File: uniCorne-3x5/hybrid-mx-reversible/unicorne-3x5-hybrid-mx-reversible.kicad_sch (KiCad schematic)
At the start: 87 parts, among them J1 MJ-4PP-9, J2 Nice!View, J3 Conn_01x02, J3 Conn_01x03, SW1 SW_MX_HS, SW10 SW_MX_HS, SW11 SW_MX_HS, SW12 SW_MX_HS, SW13 SW_MX_HS, SW14 SW_MX_HS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

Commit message: amended hybrid 3x5
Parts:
- U1: footprint TB2086_MISC:ProMicro-ish-dn-rev-unrouted_3x5 -> TB2086_MISC:ProMicro-ish-dn-rev-unrouted_3x6
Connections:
- net BAT+: now also PSW1.1 (A); no longer PSW1.3 (C)

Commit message: fixed footprint for promicro-ish 3x6
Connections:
- net CS: now also U1.12 (B5); no longer U1.13 (B6)
- net IS_LEFT: now also U1.13 (B6); no longer U1.12 (B5)
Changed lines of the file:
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@@
     )
   )
-  (global_label "CS" (shape input) (at 80.645 54.61 0) (fields_autoplaced)
+  (global_label "IS_LEFT" (shape input) (at 80.645 54.61 0) (fields_autoplaced)
     (effects (font (size 1.1938 1.1938)) (justify left))
-    (property "Intersheetrefs" "${INTERSHEET_REFS}" (at 85.7069 54.61 0)
+    (property "Intersheetrefs" "${INTERSHEET_REFS}" (at 89.9706 54.61 0)
       (effects (font (size 1.27 1.27)) (justify left) hide)
     )
@@
     )
   )
-  (global_label "IS_LEFT" (shape input) (at 36.83 54.61 180) (fields_autoplaced)
+  (global_label "CS" (shape input) (at 36.83 54.61 180) (fields_autoplaced)
     (effects (font (size 1.1938 1.1938)) (justify right))
-    (property "Intersheetrefs" "${INTERSHEET_REFS}" (at 27.5044 54.61 0)
+    (property "Intersheetrefs" "${INTERSHEET_REFS}" (at 31.7681 54.61 0)
       (effects (font (size 1.27 1.27)) (justify right) hide)
     )

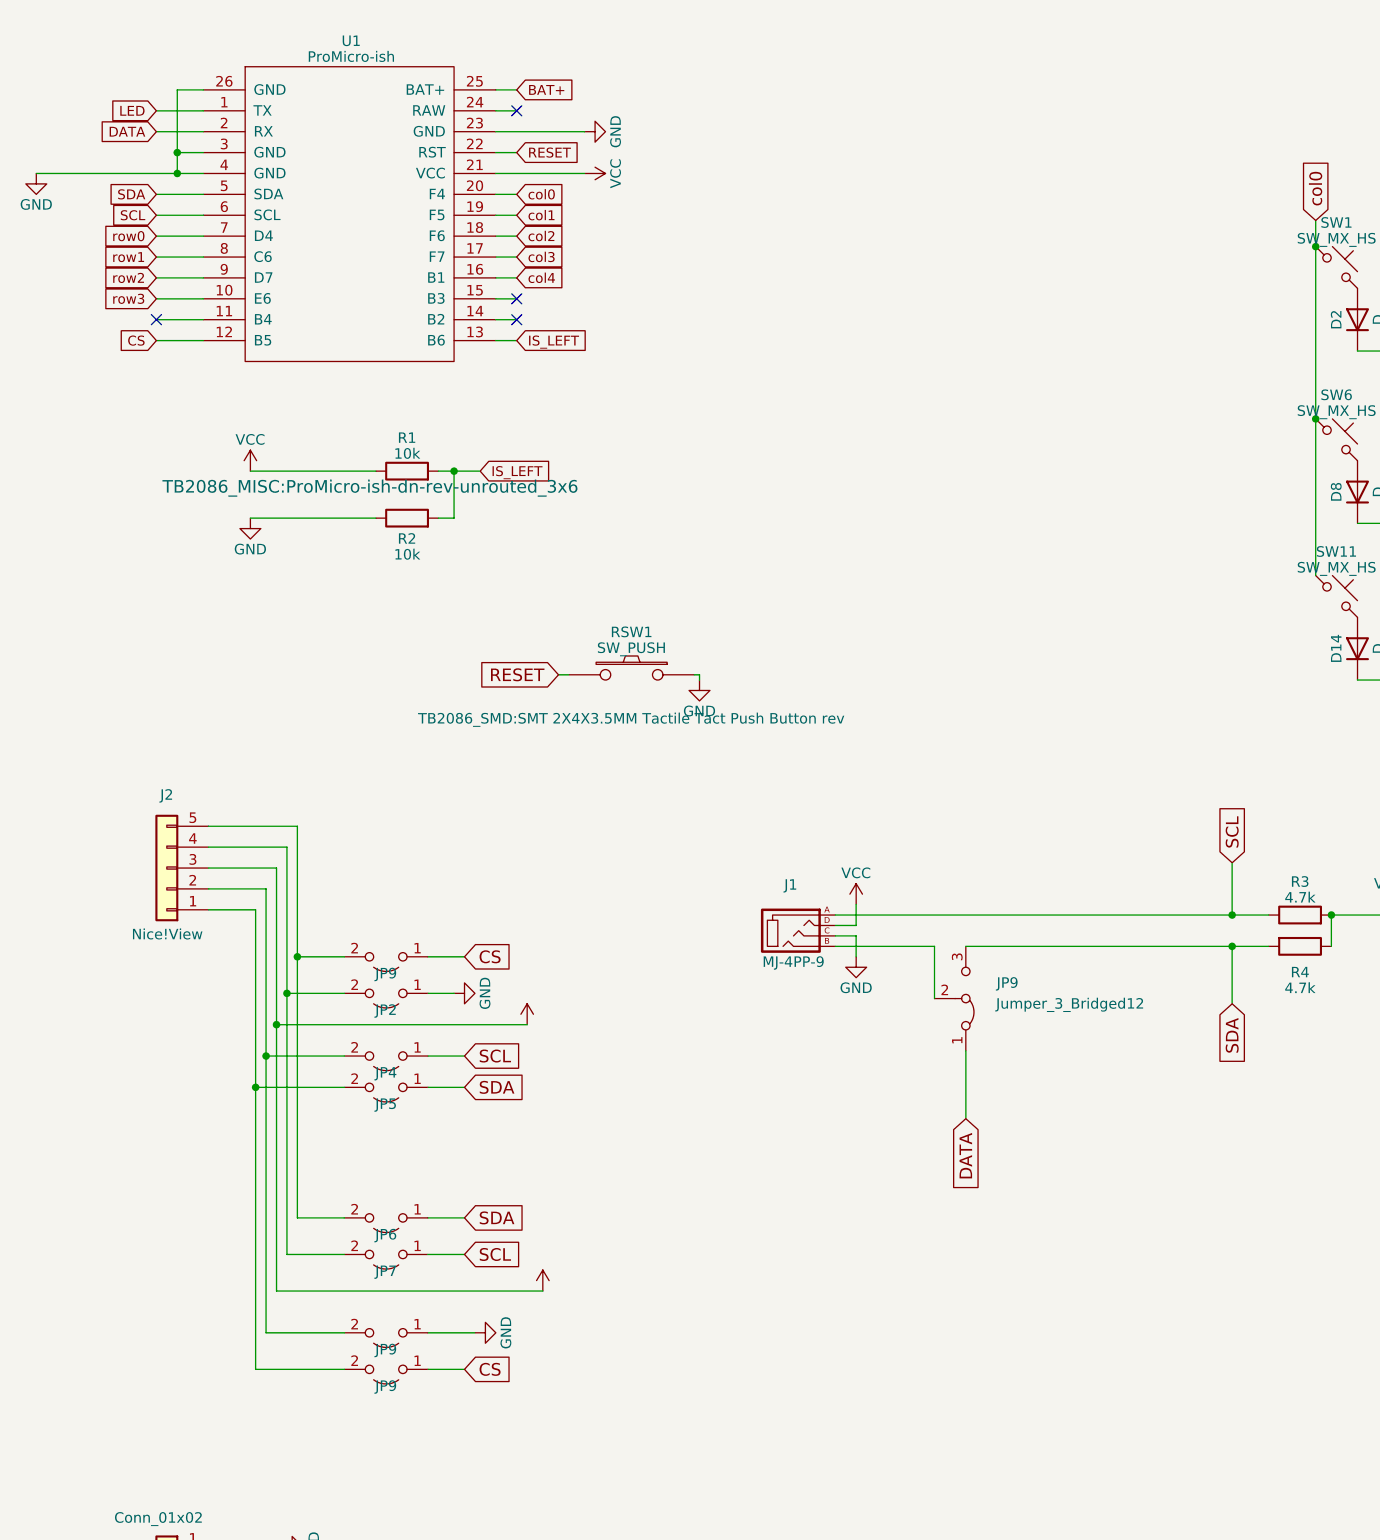
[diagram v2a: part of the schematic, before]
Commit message: Bug fix scl (#3)
* fixed 3x5 hyprid mx

* fixed 3x5

* fixed 3x6
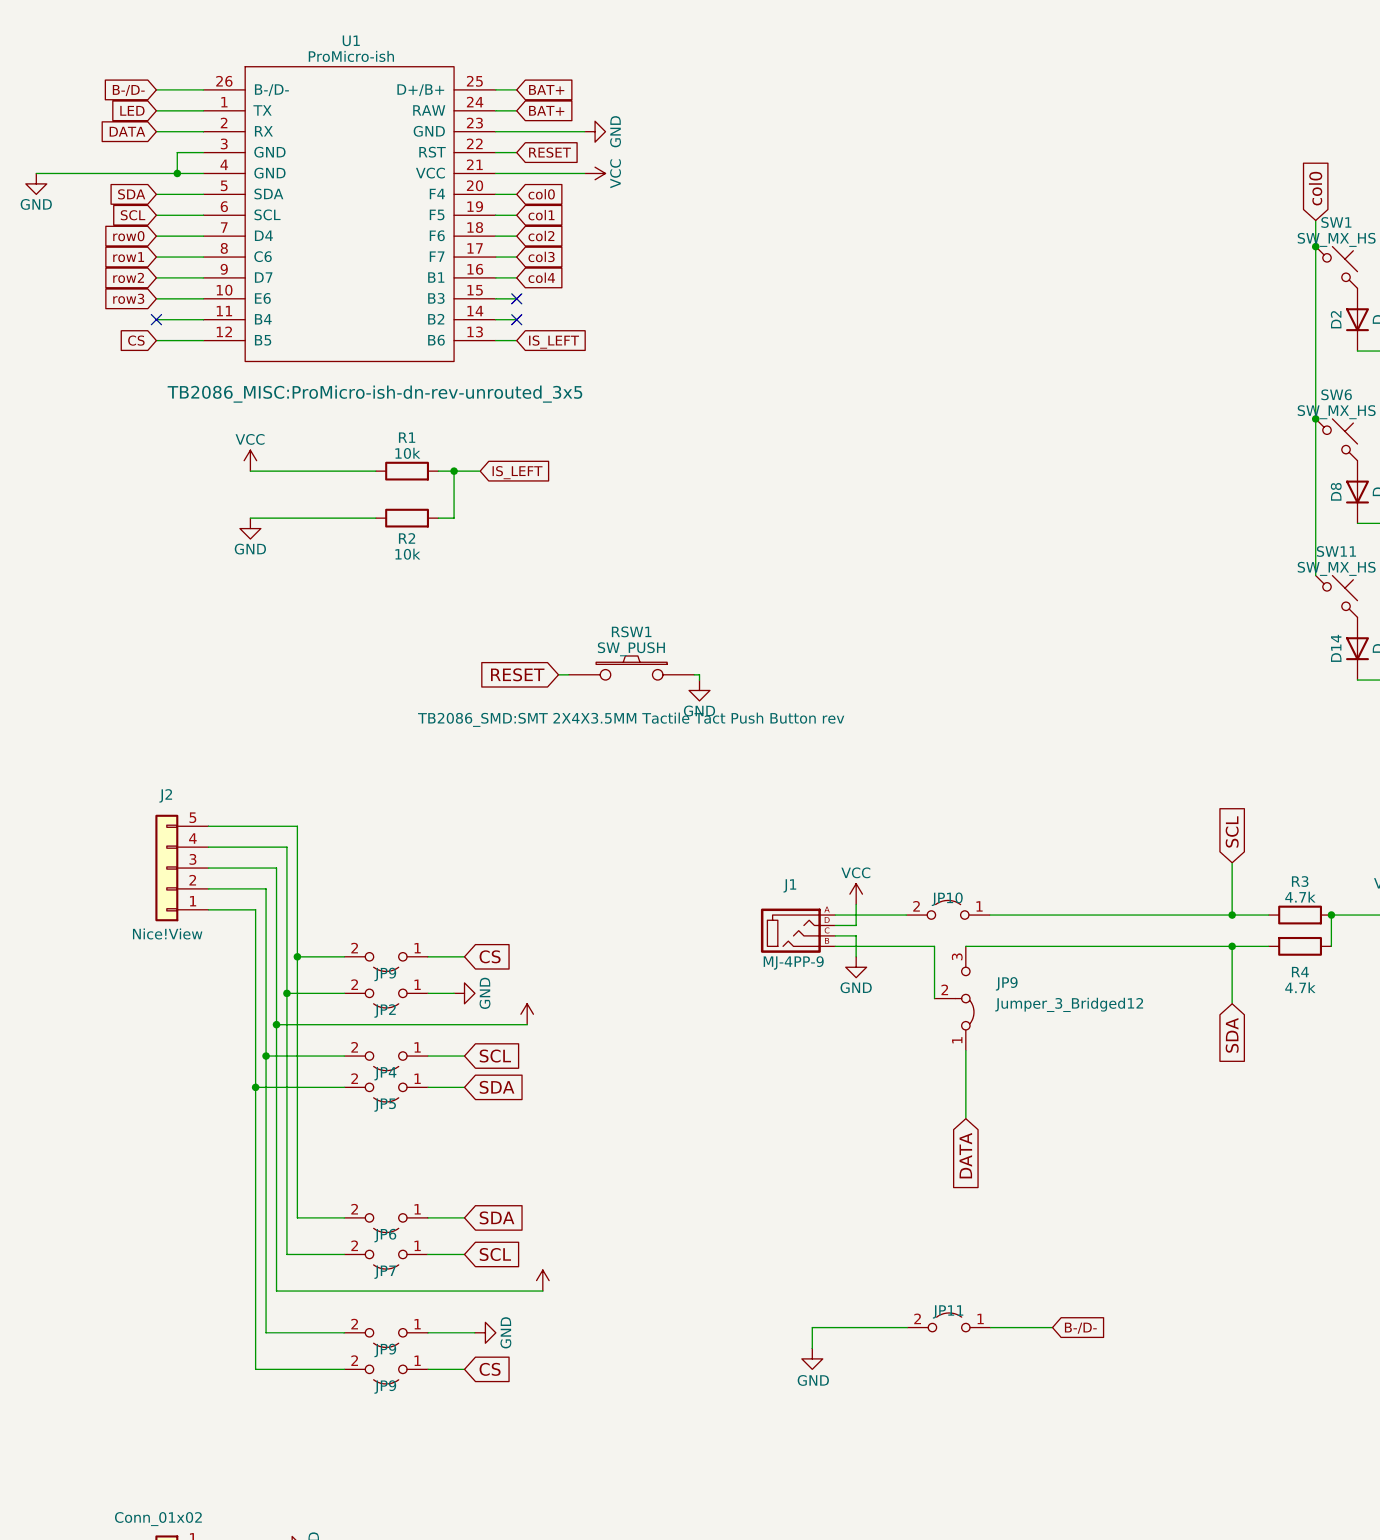
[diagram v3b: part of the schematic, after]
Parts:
- added JP10, JP11: (no value), TB2086_MISC:SolderJumper-2_P1.3mm_Open_TrianglePad1.0x1.2mm_rev, symbol Jumper:Jumper_2_Open
- U1: footprint TB2086_MISC:ProMicro-ish-dn-rev-unrouted_3x6 -> TB2086_MISC:ProMicro-ish-dn-rev-unrouted_3x5
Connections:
- net BAT+: now also U1.24 (RAW)
- net GND: now also JP11.2 (B); no longer U1.26 (GND)
- net SCL: now also JP10.1 (A); no longer J1.A
- new net: J1.A, JP10.2 (B)
- new net B-/D-: JP11.1 (A), U1.26 (B-/D-)
- no-connect marks 6 -> 5
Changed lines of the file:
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@@
   (junction (at 177.8 64.135) (diameter 0) (color 0 0 0 0)
   )
-  (junction (at 361.95 177.8) (diameter 0) (color 0 0 0 0)
-  )
   (junction (at 167.64 124.46) (diameter 0) (color 0 0 0 0)
   )
+  (junction (at 361.95 177.8) (diameter 0) (color 0 0 0 0)
+  )
   (junction (at 251.46 198.12) (diameter 0) (color 0 0 0 0)
   )
@@
   (junction (at 361.95 198.12) (diameter 0) (color 0 0 0 0)
   )
-  (junction (at 39.37 31.75) (diameter 0) (color 0 0 0 0)
-  )
   (junction (at 53.975 129.54) (diameter 0) (color 0 0 0 0)
   )
@@
   )
   (no_connect (at 36.83 52.07))
-  (no_connect (at 80.645 26.67))
   (no_connect (at 261.62 168.91))
   (no_connect (at 59.69 208.915))
@@
     (stroke (width 0) (type default))
   )
-  (wire (pts (xy 119.38 124.46) (xy 167.64 124.46))
-    (stroke (width 0) (type default))
-  )
   (wire (pts (xy 318.77 152.4) (xy 346.71 152.4))
     (stroke (width 0) (type default))
@@
     (stroke (width 0) (type default))
   )
+  (wire (pts (xy 116.586 177.165) (xy 116.586 174.625))
+    (stroke (width 0) (type default))
+  )
   (wire (pts (xy 78.105 34.29) (xy 88.9 34.29))
     (stroke (width 0) (type default))
@@
     (stroke (width 0) (type default))
   )
-  (wire (pts (xy 39.37 24.13) (xy 39.37 31.75))
-    (stroke (width 0) (type default))
-  )
   (wire (pts (xy 257.81 95.885) (xy 254 95.885))
     (stroke (width 0) (type default))
@@
     (stroke (width 0) (type default))
   )
+  (wire (pts (xy 138.176 124.46) (xy 167.64 124.46))
+    (stroke (width 0) (type default))
+  )
   (wire (pts (xy 354.33 120.65) (xy 363.22 120.65))
     (stroke (width 0) (type default))
@@
     (stroke (width 0) (type default))
   )
-  (wire (pts (xy 42.545 24.13) (xy 39.37 24.13))
+  (wire (pts (xy 36.83 24.13) (xy 42.545 24.13))
     (stroke (width 0) (type default))
   )
@@
     (stroke (width 0) (type default))
   )
+  (wire (pts (xy 138.303 174.625) (xy 145.796 174.625))
+    (stroke (width 0) (type default))
+  )
   (wire (pts (xy 251.46 217.17) (xy 251.46 222.25))
     (stroke (width 0) (type default))
@@
     (stroke (width 0) (type default))
   )
+  (wire (pts (xy 119.38 124.46) (xy 128.016 124.46))
+    (stroke (width 0) (type default))
+  )
   (wire (pts (xy 351.79 198.12) (xy 361.95 198.12))
     (stroke (width 0) (type default))
@@
     (stroke (width 0) (type default))
   )
+  (wire (pts (xy 116.586 174.625) (xy 128.143 174.625))
+    (stroke (width 0) (type default))
+  )
   (wire (pts (xy 48.895 123.825) (xy 48.895 145.415))
     (stroke (width 0) (type default))
@@
   (global_label "BAT+" (shape input) (at 80.645 24.13 0) (fields_autoplaced)
     (effects (font (size 1.1938 1.1938)) (justify left))
-    (property "Intersheetrefs" "${INTERSHEET_REFS}" (at 87.9808 24.13 0)
+    (property "Intersheetrefs" "${INTERSHEET_REFS}" (at 88.0554 24.13 0)
       (effects (font (size 1.27 1.27)) (justify left) hide)
     )
@@
     )
   )
+  (global_label "BAT+" (shape input) (at 80.645 26.67 0) (fields_autoplaced)
+    (effects (font (size 1.1938 1.1938)) (justify left))
+    (property "Intersheetrefs" "${INTERSHEET_REFS}" (at 88.0554 26.67 0)
+      (effects (font (size 1.27 1.27)) (justify left) hide)
+    )
+  )
+  (global_label "B-{slash}D-" (shape input) (at 36.83 24.13 180) (fields_autoplaced)
+    (effects (font (size 1.1938 1.1938)) (justify right))
+    (property "Intersheetrefs" "${INTERSHEET_REFS}" (at 27.4301 24.13 0)
+      (effects (font (size 1.27 1.27)) (justify right) hide)
+    )
+  )
   (global_label "CS" (shape input) (at 74.295 179.705 0) (fields_autoplaced)
     (effects (font (size 1.524 1.524)) (justify left))
@@
     )
   )
+  (global_label "B-{slash}D-" (shape input) (at 145.796 174.625 0) (fields_autoplaced)
+    (effects (font (size 1.1938 1.1938)) (justify left))
+    (property "Intersheetrefs" "${INTERSHEET_REFS}" (at 155.1959 174.625 0)
+      (effects (font (size 1.27 1.27)) (justify left) hide)
+    )
+  )
   (global_label "col2" (shape input) (at 80.645 41.91 0) (fields_autoplaced)
     (effects (font (size 1.1938 1.1938)) (justify left))
@@
       (effects (font (size 1.27 1.27)))
     )
-    (property "Footprint" "TB2086_MISC:ProMicro-ish-dn-rev-unrouted_3x6" (at 62.865 72.39 0)
+    (property "Footprint" "TB2086_MISC:ProMicro-ish-dn-rev-unrouted_3x5" (at 63.5 60.96 0)
       (effects (font (size 1.524 1.524)))
     )
@@
     )
   )
+  (symbol (lib_id "Jumper:Jumper_2_Open") (at 133.223 174.625 0) (mirror y) (unit 1)
+    (in_bom yes) (on_board yes) (dnp no)
+    (property "Reference" "JP11" (at 133.223 172.593 0)
+      (effects (font (size 1.27 1.27)))
+    )
+    (property "Value" " " (at 132.969 176.149 0)
+      (effects (font (size 1.27 1.27)))
+    )
+    (property "Footprint" "TB2086_MISC:SolderJumper-2_P1.3mm_Open_TrianglePad1.0x1.2mm_rev" (at 133.223 174.625 0)
+      (effects (font (size 1.27 1.27)) hide)
+    )
+    (property "Datasheet" "~" (at 133.223 174.625 0)
+      (effects (font (size 1.27 1.27)) hide)
+    )
+    (pin "1")
+    (pin "2")
+    (instances
+      (project "unicorne-3x5-hybrid-mx-reversible"
+        (path "/ea5c1f8d-7557-4cbf-a5a2-ee0a51c138e9"
+          (reference "JP11") (unit 1)
+        )
+      )
+    )
+  )
   (symbol (lib_id "Device:D") (at 182.88 92.075 90) (unit 1)
     (in_bom yes) (on_board yes) (dnp no)
@@
     )
   )
+  (symbol (lib_id "Jumper:Jumper_2_Open") (at 133.096 124.46 0) (mirror y) (unit 1)
+    (in_bom yes) (on_board yes) (dnp no)
+    (property "Reference" "JP10" (at 133.096 122.428 0)
+      (effects (font (size 1.27 1.27)))
+    )
+    (property "Value" " " (at 132.842 125.984 0)
+      (effects (font (size 1.27 1.27)))
+    )
+    (property "Footprint" "TB2086_MISC:SolderJumper-2_P1.3mm_Open_TrianglePad1.0x1.2mm_rev" (at 133.096 124.46 0)
+      (effects (font (size 1.27 1.27)) hide)
+    )
+    (property "Datasheet" "~" (at 133.096 124.46 0)
+      (effects (font (size 1.27 1.27)) hide)
+    )
+    (pin "1")
+    (pin "2")
+    (instances
+      (project "unicorne-3x5-hybrid-mx-reversible"
+        (path "/ea5c1f8d-7557-4cbf-a5a2-ee0a51c138e9"
+          (reference "JP10") (unit 1)
+        )
+      )
+    )
+  )
   (symbol (lib_id "power:GND") (at 391.16 133.35 0) (unit 1)
     (in_bom yes) (on_board yes) (dnp no) (fields_autoplaced)
@@
         )
       )
+    )
+  )
+  (symbol (lib_id "power:GND") (at 116.586 177.165 0) (mirror y) (unit 1)
+    (in_bom yes) (on_board yes) (dnp no)
+    (property "Reference" "#PWR010" (at 116.586 183.515 0)
+      (effects (font (size 1.27 1.27)) hide)
+    )
+    (property "Value" "GND" (at 116.713 181.102 0)
+      (effects (font (size 1.27 1.27)))
+    )
+    (property "Footprint" "" (at 116.586 177.165 0)
+      (effects (font (size 1.27 1.27)) hide)
+    )
+    (property "Datasheet" "" (at 116.586 177.165 0)
+      (effects (font (size 1.27 1.27)) hide)
+    )
+    (pin "1")
+    (instances
+      (project "unicorne-3x5-hybrid-mx-reversible"
+        (path "/ea5c1f8d-7557-4cbf-a5a2-ee0a51c138e9"
+          (reference "#PWR010") (unit 1)
+        )
+      )

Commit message: KiCAD 8
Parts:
- JP10, JP11, JP2, JP4, JP5, JP6, JP7, JP9: value (none) -> (none)
